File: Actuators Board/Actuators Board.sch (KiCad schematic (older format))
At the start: 73 parts, among them J10 Conn_01x02_Male, J9 Conn_01x02_Male, Q1 MMDT2222A

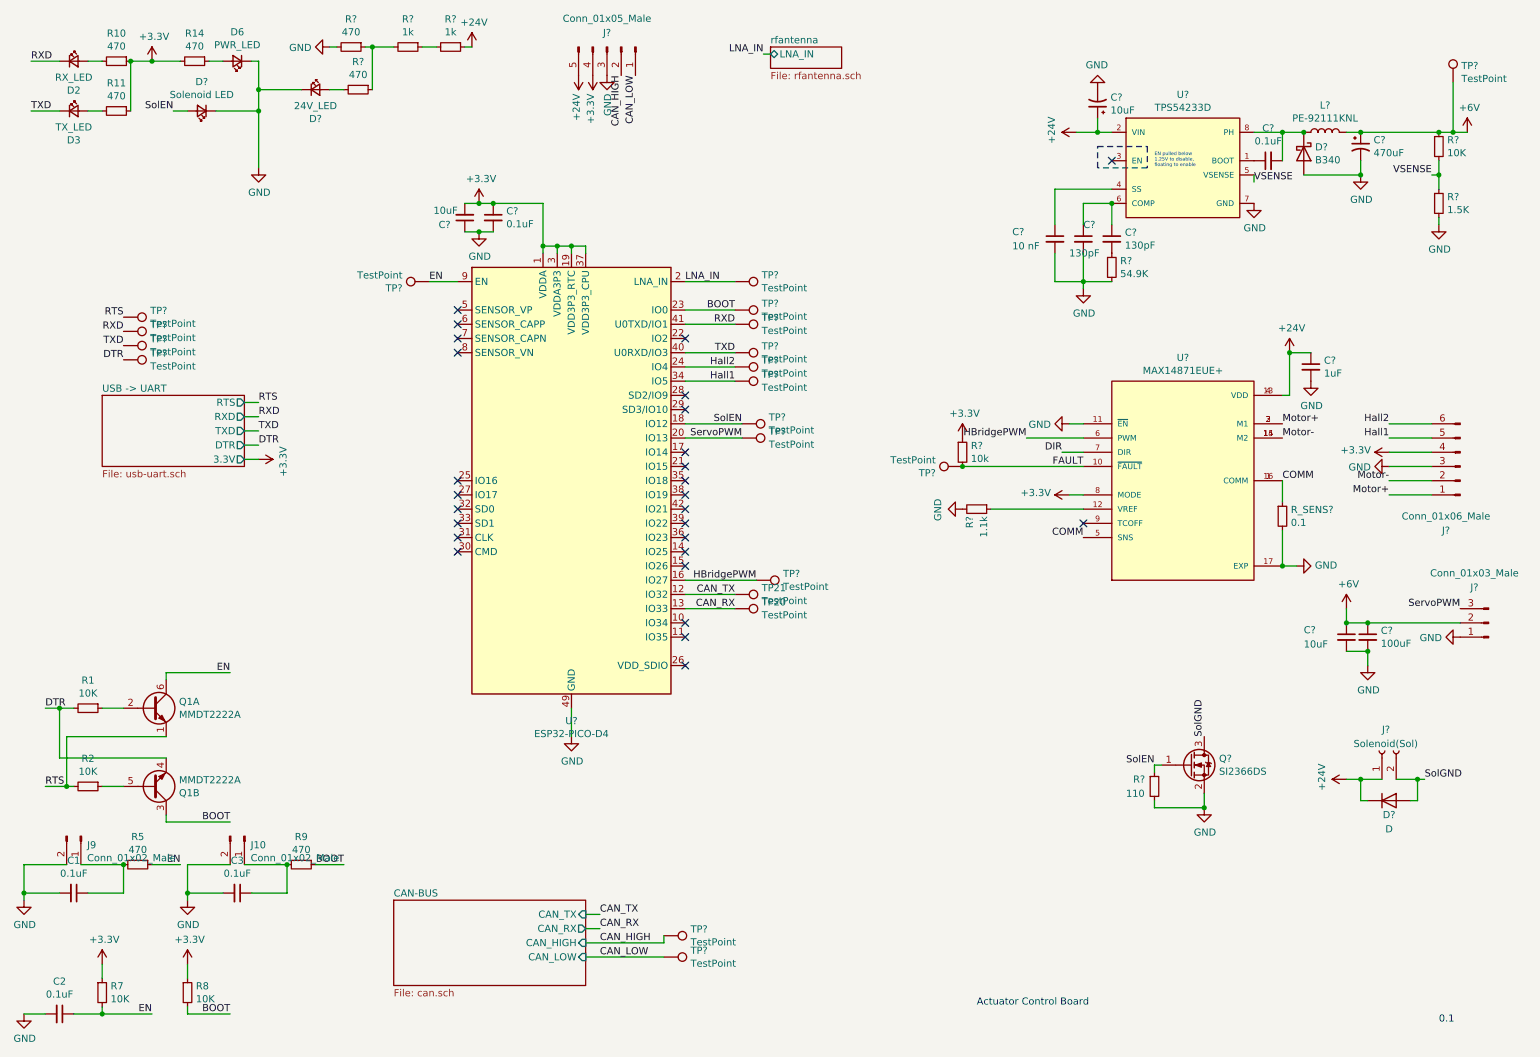
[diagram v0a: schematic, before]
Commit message: Assigned footprints, changed sense resistor value, added diode to UART
Sense resistor on the buck converter changed from 1.5K to 1.54K to more closely match 6V. Also added a diode on the 3.3V output on the USB-UART converter.
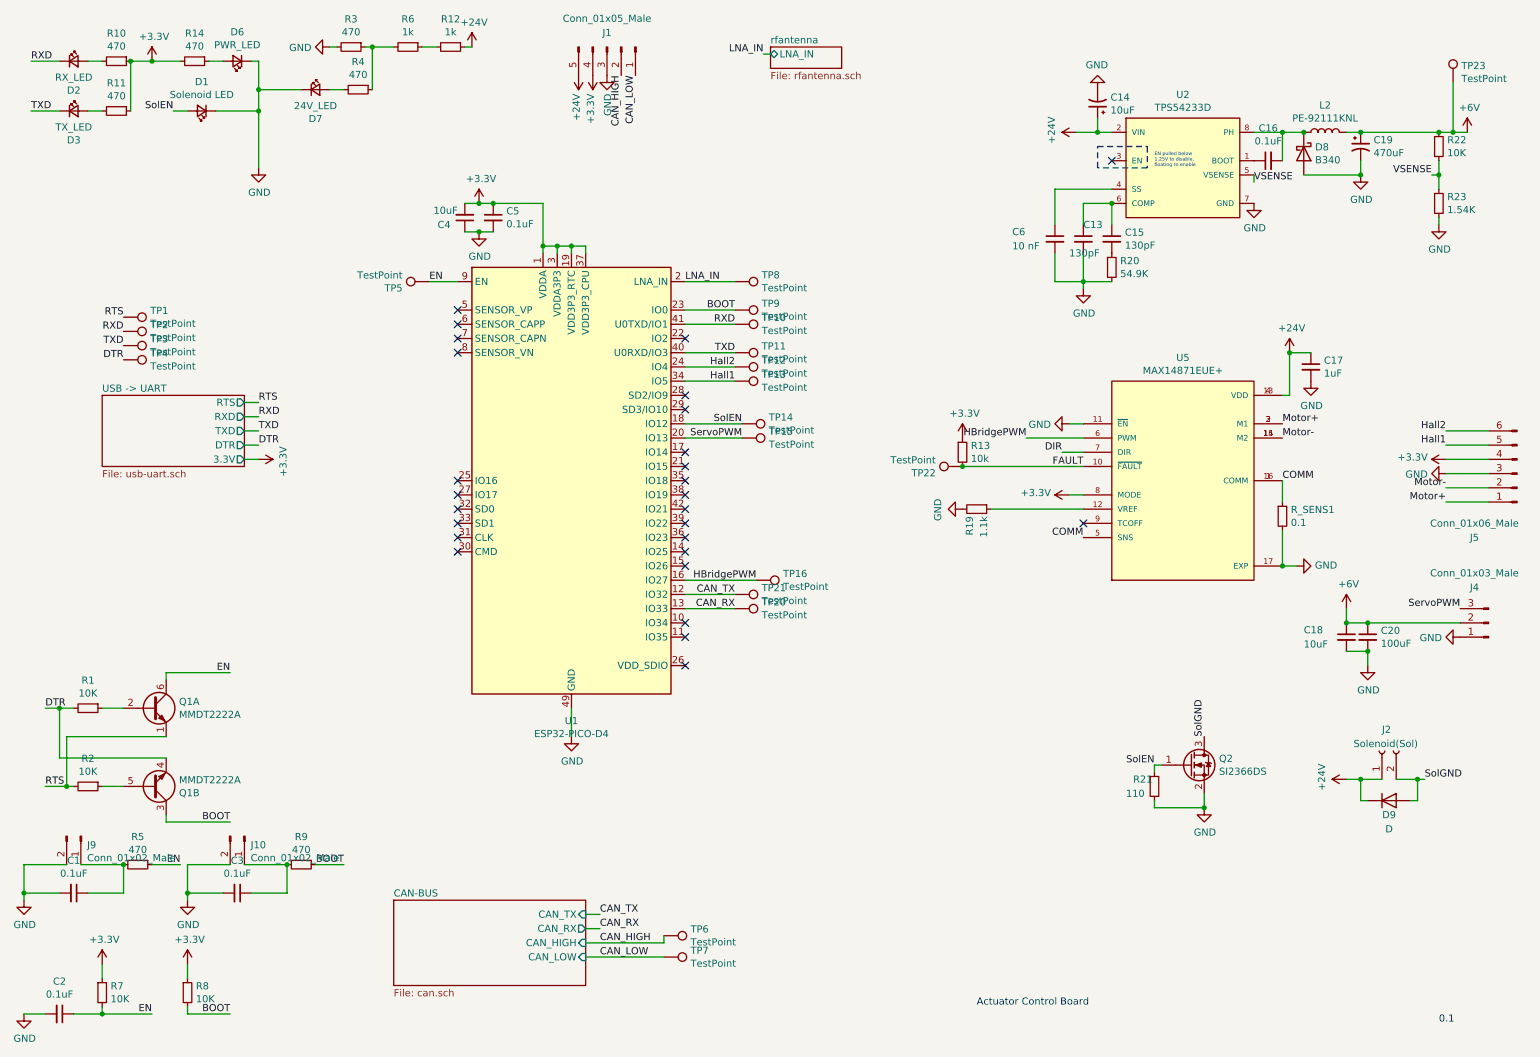
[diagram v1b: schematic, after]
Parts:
- C13, C14, C15, C16, C18, C20, C4, C5, C6: renamed from C?; footprint (none) -> Capacitor_SMD:C_0603_1608Metric
- C19: renamed from C?; footprint (none) -> Capacitor_SMD:CP_Elec_8x6.7
- D9: renamed from D?; footprint (none) -> Diode_SMD:D_0603_1608Metric_Castellated
- L2: renamed from L?; footprint (none) -> Inductor_SMD:L_12x12mm_H6mm
- R20, R21, R22: renamed from R?; footprint (none) -> Resistor_SMD:R_0603_1608Metric
- R23: renamed from R?; value 1.5K -> 1.54K; footprint (none) -> Resistor_SMD:R_0603_1608Metric
- TP10, TP11, TP14, TP15, TP23, TP5, TP6, TP7, TP8, TP9: renamed from TP?; footprint (none) -> TestPoint:TestPoint_THTPad_1.0x1.0mm_Drill0.5mm
- U2: renamed from U?; footprint Texas_Instruments-TPS54233D-* -> iclr:SOIC127P599X175-8N
- gave numbers to parts that had none: 26
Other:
- moved on the sheet: J5

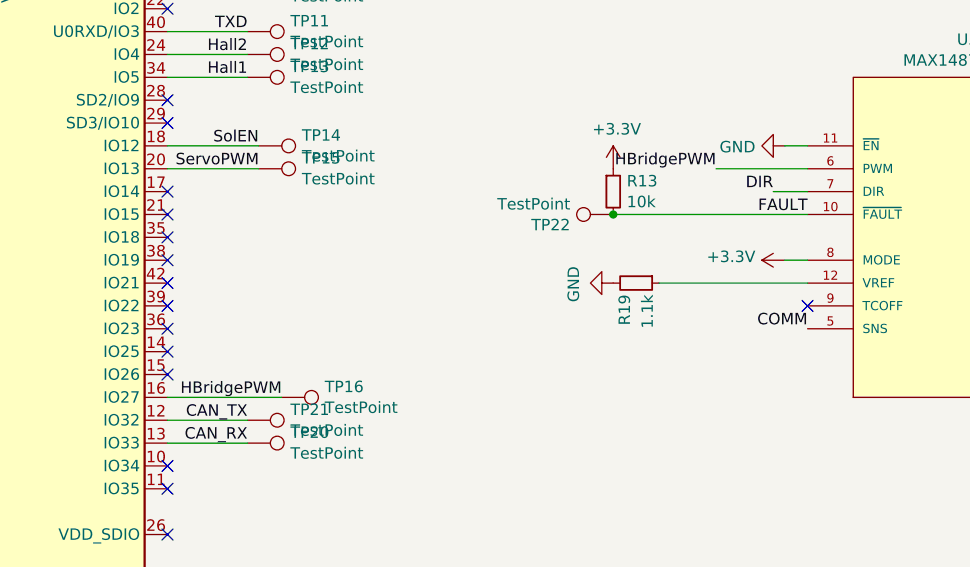
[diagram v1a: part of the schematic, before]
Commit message: Connected H bridge direction select pin to esp32(I forgor)
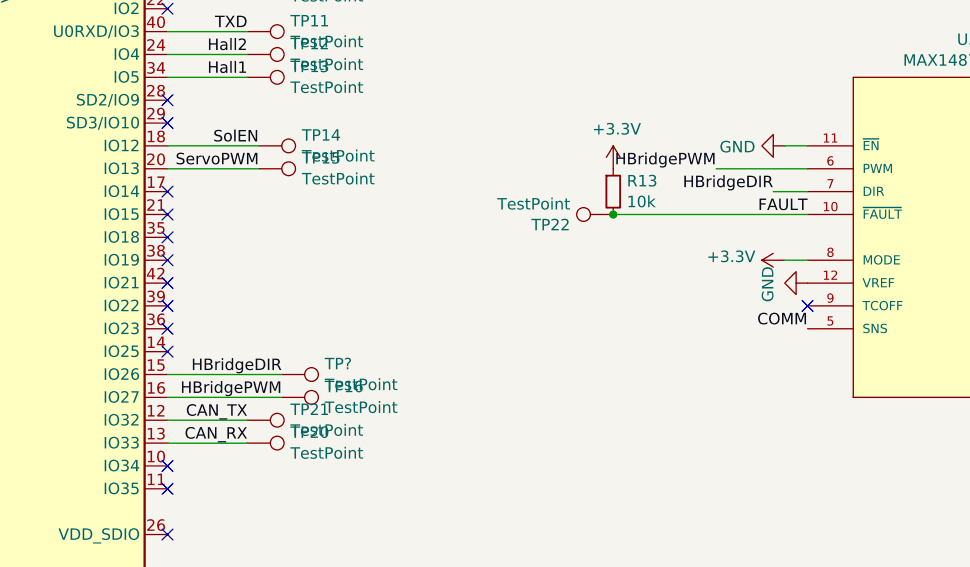
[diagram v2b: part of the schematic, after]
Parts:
- removed R19: 1.1k, Resistor_SMD:R_0603_1608Metric, symbol Device:R_Small
- added TP?: TestPoint, TestPoint:TestPoint_THTPad_1.0x1.0mm_Drill0.5mm, symbol Connector:TestPoint
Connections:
- net DIR is gone; now on net HBridgeDIR: U5.7 (DIR)
- net GND: now also U5.12 (VREF)
- net HBridgeDIR: now reaches U1.15 (IO26)
- net HBridgeDIR: now also TP?.1
- no-connect marks 27 -> 26
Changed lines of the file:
@@
 NoConn ~ 5300 4100
 NoConn ~ 5300 4300
-NoConn ~ 5300 4400
 NoConn ~ 5300 4800
 NoConn ~ 5300 4900
@@
 	8100 3600 7950 3600
 Text Label 7950 3600 2    50   ~ 0
-DIR
+HBridgeDIR
 $Comp
 L power:GND #PWR0117
 U 1 1 61BFAAD4
-P 7250 4000
-F 0 "#PWR0117" H 7250 3750 50  0001 C CNN
-F 1 "GND" H 7255 3827 50  0000 C CNN
-F 2 "" H 7250 4000 50  0001 C CNN
-F 3 "" H 7250 4000 50  0001 C CNN
-	1    7250 4000
+P 8100 4000
+F 0 "#PWR0117" H 8100 3750 50  0001 C CNN
+F 1 "GND" H 8105 3827 50  0000 C CNN
+F 2 "" H 8100 4000 50  0001 C CNN
+F 3 "" H 8100 4000 50  0001 C CNN
+	1    8100 4000
 	0    1    1    0
 $EndComp
@@
 Wire Wire Line
 	8000 3900 8100 3900
-Wire Wire Line
-	7450 4000 8100 4000
 Text Label 9500 3400 0    50   ~ 0
 Motor+
@@
 Wire Wire Line
 	7250 3700 8100 3700
-$Comp
-L Device:R_Small R19
-U 1 1 61BFAB38
-P 7350 4000
-F 0 "R19" H 7400 3950 50  0000 L CNN
-F 1 "1.1k" H 7400 4050 50  0000 L CNN
-F 2 "Resistor_SMD:R_0603_1608Metric" H 7350 4000 50  0001 C CNN
-F 3 "~" H 7350 4000 50  0001 C CNN
-	1    7350 4000
-	0    1    1    0
-$EndComp
 Text Label 5650 3100 2    50   ~ 0
 Hall1
@@
 Wire Wire Line
 	2300 1200 2300 1600
+Wire Wire Line
+	5300 4400 5800 4400
+Text Label 5800 4400 2    50   ~ 0
+HBridgeDIR
+$Comp
+L Connector:TestPoint TP?
+U 1 1 61CE8ABF
+P 5800 4400
+F 0 "TP?" V 5754 4588 50  0000 L CNN
+F 1 "TestPoint" V 5845 4588 50  0000 L CNN
+F 2 "TestPoint:TestPoint_THTPad_1.0x1.0mm_Drill0.5mm" H 6000 4400 50  0001 C CNN
+F 3 "~" H 6000 4400 50  0001 C CNN
+	1    5800 4400
+	0    1    1    0
+$EndComp
 $EndSCHEMATC

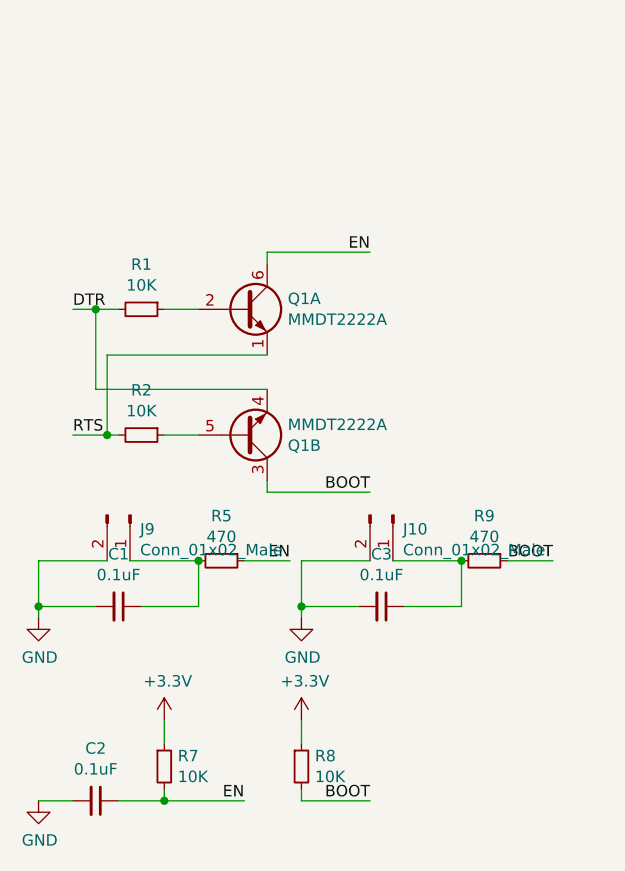
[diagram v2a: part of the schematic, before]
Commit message: Changed Pico EN capacitor to 1 uF (spotted in the datasheet)
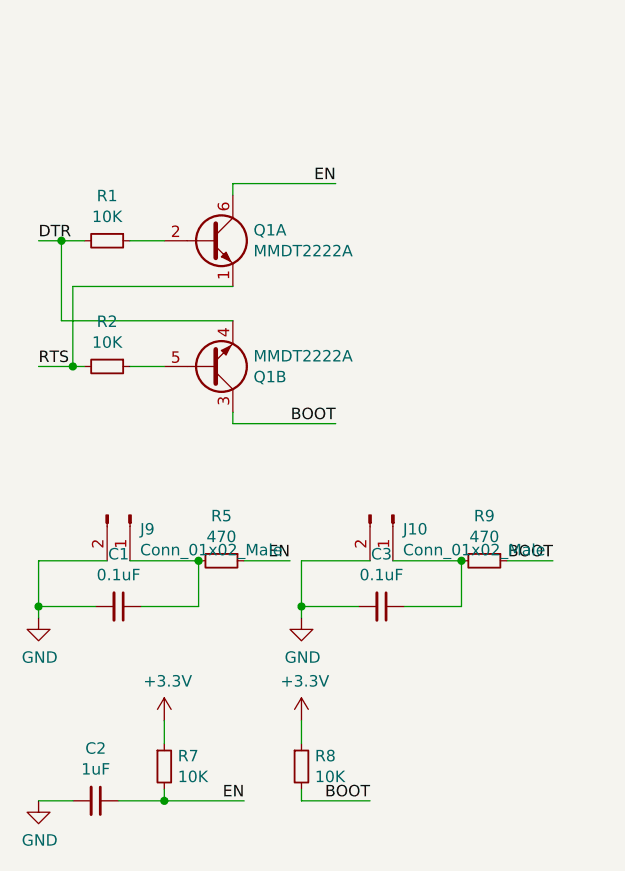
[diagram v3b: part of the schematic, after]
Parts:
- C2: value 0.1uF -> 1uF
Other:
- moved on the sheet: Q1A, Q1B, R1, R2
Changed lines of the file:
@@
 P 900 7550
 F 0 "C2" V 671 7550 50  0000 C CNN
-F 1 "0.1uF" V 762 7550 50  0000 C CNN
+F 1 "1uF" V 762 7550 50  0000 C CNN
 F 2 "Capacitor_SMD:C_0603_1608Metric" H 900 7550 50  0001 C CNN
 F 3 "~" H 900 7550 50  0001 C CNN
@@
 	1200 7200 1200 7300
 Wire Wire Line
-	1650 5200 1650 5150
-Wire Wire Line
-	1650 5150 2100 5150
-Wire Wire Line
-	1650 6150 1650 6200
-Wire Wire Line
-	1650 6200 2100 6200
+	1500 4900 1500 4850
+Wire Wire Line
+	1500 4850 1950 4850
+Wire Wire Line
+	1500 5850 1500 5900
+Wire Wire Line
+	1500 5900 1950 5900
 $Comp
 L Device:R_Small R1
 U 1 1 5DB9F807
-P 1100 5400
-F 0 "R1" V 904 5400 50  0000 C CNN
-F 1 "10K" V 995 5400 50  0000 C CNN
-F 2 "Resistor_SMD:R_0603_1608Metric" H 1100 5400 50  0001 C CNN
-F 3 "~" H 1100 5400 50  0001 C CNN
-	1    1100 5400
+P 950 5100
+F 0 "R1" V 754 5100 50  0000 C CNN
+F 1 "10K" V 845 5100 50  0000 C CNN
+F 2 "Resistor_SMD:R_0603_1608Metric" H 950 5100 50  0001 C CNN
+F 3 "~" H 950 5100 50  0001 C CNN
+	1    950  5100
 	0    1    1    0
 $EndComp
@@
 L Device:R_Small R2
 U 1 1 5DBA0737
-P 1100 5950
-F 0 "R2" V 904 5950 50  0000 C CNN
-F 1 "10K" V 995 5950 50  0000 C CNN
-F 2 "Resistor_SMD:R_0603_1608Metric" H 1100 5950 50  0001 C CNN
-F 3 "~" H 1100 5950 50  0001 C CNN
-	1    1100 5950
-	0    1    1    0
-$EndComp
-Wire Wire Line
-	1200 5950 1350 5950
-Wire Wire Line
-	1350 5400 1200 5400
-Wire Wire Line
-	1000 5950 950  5950
-Wire Wire Line
-	1000 5400 900  5400
-Wire Wire Line
-	950  5950 950  5600
-Wire Wire Line
-	950  5600 1650 5600
-Connection ~ 950  5950
-Wire Wire Line
-	950  5950 800  5950
-Wire Wire Line
-	900  5400 900  5750
-Wire Wire Line
-	900  5750 1650 5750
-Connection ~ 900  5400
-Wire Wire Line
-	900  5400 800  5400
-Text Label 800  5400 0    50   ~ 0
+P 950 5650
+F 0 "R2" V 754 5650 50  0000 C CNN
+F 1 "10K" V 845 5650 50  0000 C CNN
+F 2 "Resistor_SMD:R_0603_1608Metric" H 950 5650 50  0001 C CNN
+F 3 "~" H 950 5650 50  0001 C CNN
+	1    950  5650
+	0    1    1    0
+$EndComp
+Wire Wire Line
+	1050 5650 1200 5650
+Wire Wire Line
+	1200 5100 1050 5100
+Wire Wire Line
+	850  5650 800  5650
+Wire Wire Line
+	850  5100 750  5100
+Wire Wire Line
+	800  5650 800  5300
+Wire Wire Line
+	800  5300 1500 5300
+Connection ~ 800  5650
+Wire Wire Line
+	800  5650 650  5650
+Wire Wire Line
+	750  5100 750  5450
+Wire Wire Line
+	750  5450 1500 5450
+Connection ~ 750  5100
+Wire Wire Line
+	750  5100 650  5100
+Text Label 650  5100 0    50   ~ 0
 DTR
-Text Label 800  5950 0    50   ~ 0
+Text Label 650  5650 0    50   ~ 0
 RTS
-Text Label 2100 5150 2    50   ~ 0
+Text Label 1950 4850 2    50   ~ 0
 EN
-Text Label 2100 6200 2    50   ~ 0
+Text Label 1950 5900 2    50   ~ 0
 BOOT
 $Comp
@@
 L Transistor_BJT:MMDT2222A Q1
 U 1 1 5E4F19D5
-P 1550 5400
-F 0 "Q1" H 1740 5446 50  0000 L CNN
-F 1 "MMDT2222A" H 1740 5355 50  0000 L CNN
-F 2 "Package_TO_SOT_SMD:SOT-363_SC-70-6" H 1750 5500 50  0001 C CNN
-F 3 "http://www.diodes.com/_files/datasheets/ds30125.pdf" H 1550 5400 50  0001 C CNN
-	1    1550 5400
+P 1400 5100
+F 0 "Q1" H 1590 5146 50  0000 L CNN
+F 1 "MMDT2222A" H 1590 5055 50  0000 L CNN
+F 2 "Package_TO_SOT_SMD:SOT-363_SC-70-6" H 1600 5200 50  0001 C CNN
+F 3 "http://www.diodes.com/_files/datasheets/ds30125.pdf" H 1400 5100 50  0001 C CNN
+	1    1400 5100
 	1    0    0    -1
 $EndComp
@@
 L Transistor_BJT:MMDT2222A Q1
 U 2 1 5E4F3D62
-P 1550 5950
-F 0 "Q1" H 1740 5996 50  0000 L CNN
-F 1 "MMDT2222A" H 1740 5905 50  0000 L CNN
-F 2 "Package_TO_SOT_SMD:SOT-363_SC-70-6" H 1750 6050 50  0001 C CNN
-F 3 "http://www.diodes.com/_files/datasheets/ds30125.pdf" H 1550 5950 50  0001 C CNN
-	2    1550 5950
+P 1400 5650
+F 0 "Q1" H 1590 5696 50  0000 L CNN
+F 1 "MMDT2222A" H 1590 5605 50  0000 L CNN
+F 2 "Package_TO_SOT_SMD:SOT-363_SC-70-6" H 1600 5750 50  0001 C CNN
+F 3 "http://www.diodes.com/_files/datasheets/ds30125.pdf" H 1400 5650 50  0001 C CNN
+	2    1400 5650
 	1    0    0    1
 $EndComp
